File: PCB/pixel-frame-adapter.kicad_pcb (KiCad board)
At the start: 2 copper layers, 38.9 x 41.9 mm, 4 parts, among them U1 Adafruit_1_54in_TFT, U2 Adafruit_ItsyBitsy_M4, U3 Adafruit_LIS3DH

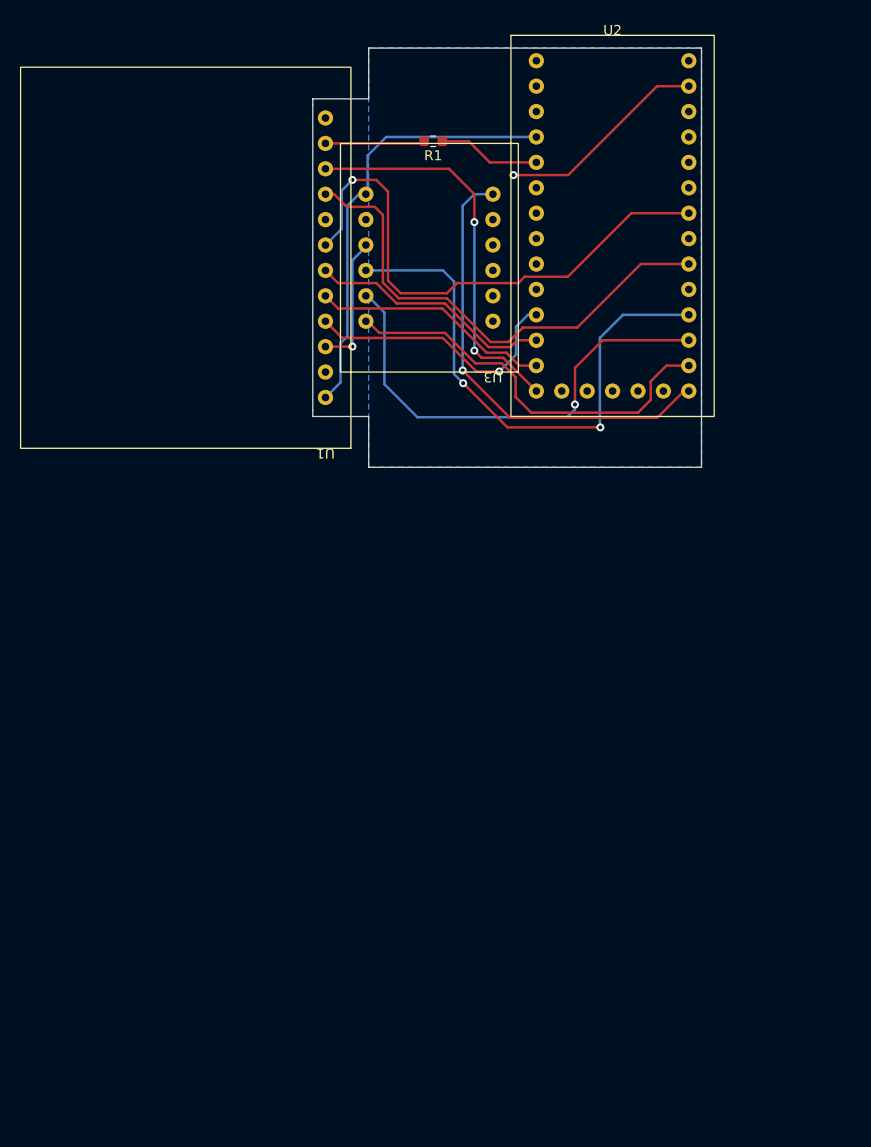
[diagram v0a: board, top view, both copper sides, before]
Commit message: rotate USB port
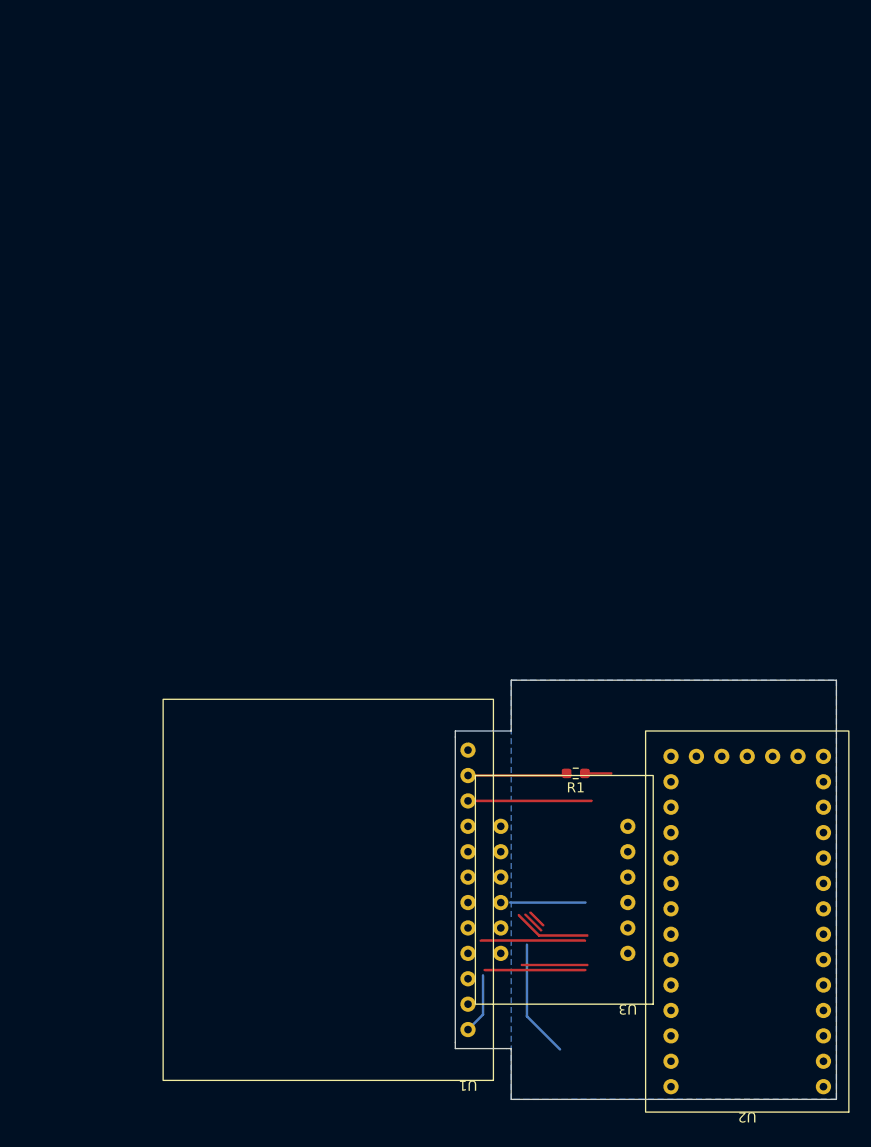
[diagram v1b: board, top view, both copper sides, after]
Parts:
- moved U2 108.5 mm to (160.8, 122.9), turned to 180 degrees
- moved R1 64.8 mm to (143.6, 89.1)
- moved U1 64.8 mm to (132.9, 119.7)
- moved U3 64.6 mm to (148.8, 112.1)
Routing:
- net SPI_CS: track 54.5 -> 1.80 mm, vias 1 -> 0
- net SPI_DC: track 49.6 -> 2.23 mm
- net I2C_SCL: track 54.0 -> 7.53 mm, vias 2 -> 0
- net ACC_INT2: track 46.0 -> 0.00 mm, vias 1 -> 0
- net +5V: track 44.1 -> 6.04 mm
- net I2C_SDA: track 46.9 -> 11.8 mm, vias 1 -> 0
- net GND: track 34.7 -> 0.00 mm, vias 2 -> 0
- net ACC_INT: track 40.1 -> 6.56 mm
- net SD_CARD_CS: track 39.9 -> 12.4 mm, vias 2 -> 0
- net SPI_CLK: track 27.1 -> 10.1 mm, vias 1 -> 0
- net SPI_MOSI: track 24.5 -> 7.70 mm
- net SD_CARD_MISO: track 24.0 -> 10.4 mm
- net BACKLIGHT: track 10.3 -> 2.64 mm
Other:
- board size 38.9 x 41.9 mm -> 38.1 x 41.9 mm

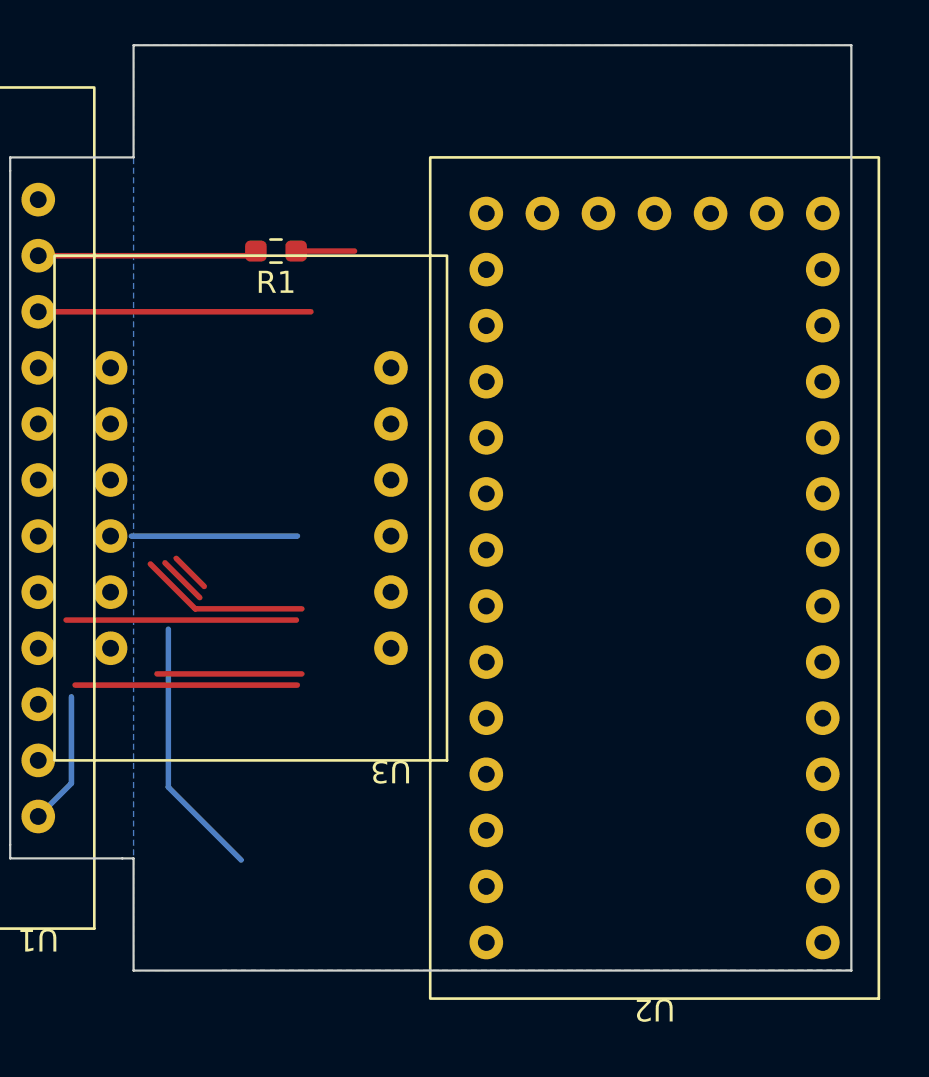
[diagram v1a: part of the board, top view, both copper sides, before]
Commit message: line up usb
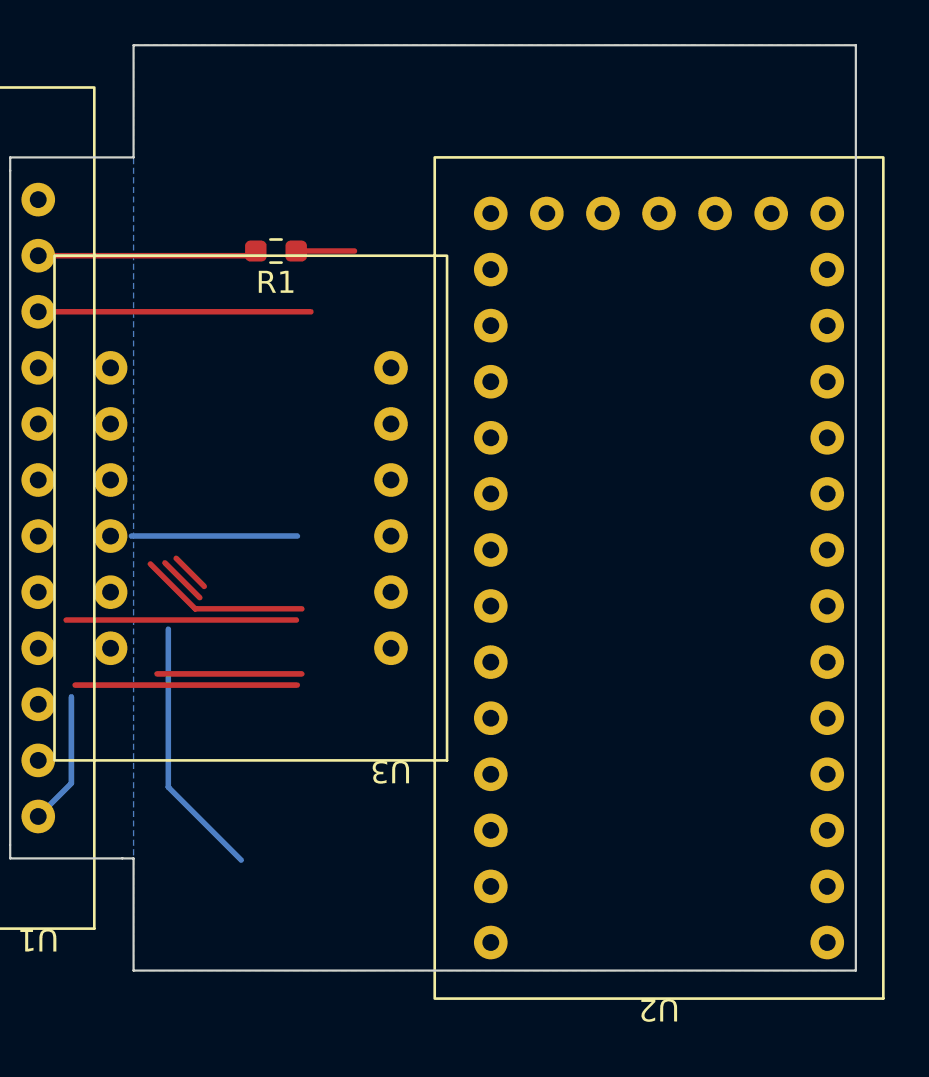
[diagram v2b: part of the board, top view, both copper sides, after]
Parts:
- moved U2 0.20 mm to (161.0, 122.9)
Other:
- board size 38.1 x 41.9 mm -> 38.3 x 41.9 mm
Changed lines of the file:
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@@
   (net 43 "unconnected-(U3-Pad8)")
   (footprint "Module:Adafruit_ItsyBitsy_M4" (layer "F.Cu")
-    (at 160.782 122.9106 180)
+    (at 160.9852 122.9106 180)
     (property "Sheetfile" "displayMotherboard.kicad_sch")
     (property "Sheetname" "")
@@
   (gr_line (start 131.5974 116.5606) (end 136.6774 116.5606) (layer "Edge.Cuts") (width 0.1))
   (gr_line (start 131.5974 84.8106) (end 131.5974 85.4202) (layer "Edge.Cuts") (width 0.1))
-  (gr_line (start 137.1854 121.6406) (end 169.6974 121.6406) (layer "Edge.Cuts") (width 0.1))
-  (gr_line (start 137.1854 79.7306) (end 169.6974 79.7306) (layer "Edge.Cuts") (width 0.1))
-  (gr_line (start 169.6974 79.7306) (end 169.6974 121.6406) (layer "Edge.Cuts") (width 0.1))
+  (gr_line (start 137.1854 121.6406) (end 169.9006 121.6406) (layer "Edge.Cuts") (width 0.1))
+  (gr_line (start 137.1854 79.7306) (end 169.9006 79.7306) (layer "Edge.Cuts") (width 0.1))
+  (gr_line (start 169.9006 79.7306) (end 169.9006 121.6406) (layer "Edge.Cuts") (width 0.1))
   (gr_line (start 137.1854 116.5606) (end 137.1854 121.6406) (layer "Edge.Cuts") (width 0.1))
   (segment (start 144.5495 89.0524) (end 147.193 89.0524) (width 0.25) (layer "F.Cu") (net 1))
@@
     (polygon
       (pts
-        (xy 169.6974 121.6152)
+        (xy 169.9006 121.6406)
         (xy 137.1854 121.6406)
         (xy 137.1854 79.7306)
-        (xy 169.6974 79.7306)
+        (xy 169.9006 79.7306)
       )
     )

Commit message: routing done
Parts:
- removed R1: 0, Resistor_SMD:R_0603_1608Metric_Pad0.98x0.95mm_HandSolder
- added JP1: SolderJumper_2_Bridged, Jumper:SolderJumper-2_P1.3mm_Bridged_RoundedPad1.0x1.5mm, F.Cu at (141.1, 85.7)
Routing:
- net +5V: track 6.04 -> 65.9 mm, vias 0 -> 1
- net SD_CARD_MISO: track 10.4 -> 66.2 mm, vias 0 -> 2
- net SPI_MOSI: track 7.70 -> 61.9 mm, vias 0 -> 3
- net SPI_CLK: track 10.1 -> 62.4 mm, vias 0 -> 2
- net BACKLIGHT: track 2.64 -> 50.2 mm, vias 0 -> 2
- net ACC_INT: track 6.56 -> 34.0 mm, vias 0 -> 2
- net SD_CARD_CS: track 12.4 -> 39.3 mm
- net SPI_CS: track 1.80 -> 27.7 mm, vias 0 -> 2
- net SPI_DC: track 2.23 -> 22.9 mm
- net I2C_SDA: track 11.8 -> 28.8 mm, vias 0 -> 2
- net I2C_SCL: track 7.53 -> 23.3 mm, vias 0 -> 2
- net ACC_INT2: track 0.00 -> 11.5 mm, vias 0 -> 1
- net Net-(JP1-Pad2): track 9.94 -> 9.08 mm

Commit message: small re-route
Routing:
- net SD_CARD_CS: track 39.3 -> 40.1 mm
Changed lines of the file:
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@@
   (segment (start 134.1308 95.6056) (end 133.8547 95.3295) (width 0.25) (layer "F.Cu") (net 9))
   (segment (start 150.0124 98.1456) (end 142.2908 98.1456) (width 0.25) (layer "F.Cu") (net 9))
+  (segment (start 144.8054 88.3666) (end 147.8788 85.2932) (width 0.25) (layer "F.Cu") (net 10))
   (segment (start 133.6736 91.8022) (end 132.8674 91.8022) (width 0.25) (layer "F.Cu") (net 10))
-  (segment (start 145.4404 87.7316) (end 147.8788 85.2932) (width 0.25) (layer "F.Cu") (net 10))
-  (segment (start 137.7442 87.7316) (end 133.6736 91.8022) (width 0.25) (layer "F.Cu") (net 10))
   (segment (start 166.5478 85.2932) (end 168.6052 87.3506) (width 0.25) (layer "F.Cu") (net 10))
   (segment (start 147.8788 85.2932) (end 166.5478 85.2932) (width 0.25) (layer "F.Cu") (net 10))
-  (segment (start 137.7442 87.7316) (end 145.4404 87.7316) (width 0.25) (layer "F.Cu") (net 10))
+  (segment (start 136.874 91.8022) (end 140.3096 88.3666) (width 0.25) (layer "F.Cu") (net 10))
+  (segment (start 132.8674 91.8022) (end 136.874 91.8022) (width 0.25) (layer "F.Cu") (net 10))
+  (segment (start 140.3096 88.3666) (end 144.8054 88.3666) (width 0.25) (layer "F.Cu") (net 10))
   (segment (start 153.3652 87.3506) (end 148.844 87.3506) (width 0.25) (layer "F.Cu") (net 25))
   (via (at 148.844 87.3506) (size 0.8) (drill 0.4) (layers "F.Cu" "B.Cu") (net 25))

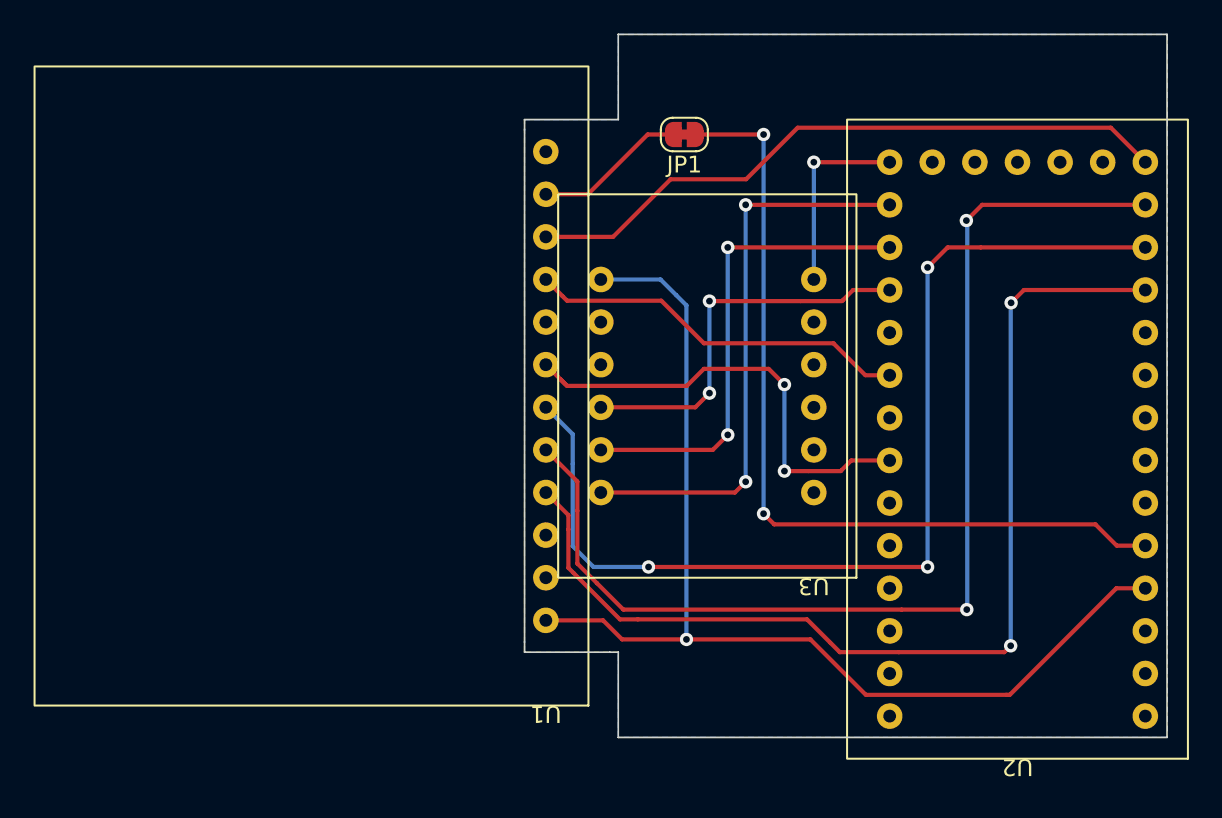
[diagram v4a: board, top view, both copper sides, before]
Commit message: dimensions and track cleanup
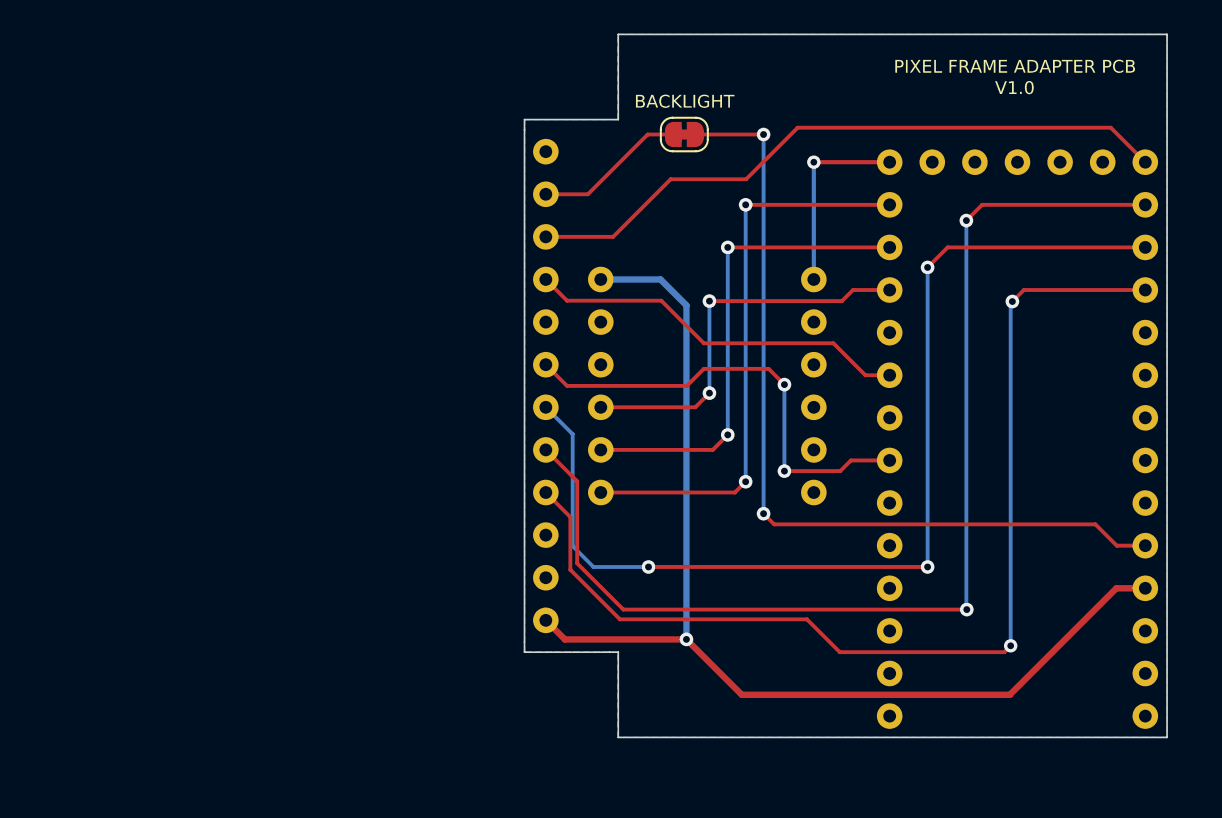
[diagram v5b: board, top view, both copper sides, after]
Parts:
- JP1: footprint Jumper:SolderJumper-2_P1.3mm_Bridged_RoundedPad1.0x1.5mm -> pixel-frame-library:SolderJumper-2_P1.3mm_Bridged_RoundedPad1.0x1.5mm
- U1: footprint Display:Adafruit_2_54in_TFT_Display -> pixel-frame-library:Adafruit_2_54in_TFT_Display
- U2: footprint Module:Adafruit_ItsyBitsy_M4 -> pixel-frame-library:Adafruit_ItsyBitsy_M4
- U3: footprint Sensor_Motion:Adafruit_LIS3DH -> pixel-frame-library:Adafruit_LIS3DH
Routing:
- net SD_CARD_CS: track 40.1 -> 39.3 mm
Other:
- board text added: "BACKLIGHT"
- board text added: "PIXEL FRAME ADAPTER PCB"
- board text added: "V1.0"

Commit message: silkscreen
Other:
- board text added: "+5V"
- board text added: "ADAFRUIT ITSYBITSY MOTHERBOARD"
- board text added: "GND"
- board text added: "LIS3DH ACCELEROMETER"
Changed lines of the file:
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@@
   (gr_line (start 169.9006 79.7306) (end 169.9006 121.6406) (layer "Edge.Cuts") (width 0.1))
   (gr_line (start 137.1854 116.5606) (end 137.1854 121.6406) (layer "Edge.Cuts") (width 0.1))
+  (gr_text "GND" (at 135.4328 109.5502) (layer "F.SilkS")
+    (effects (font (size 0.762 0.762) (thickness 0.1905)))
+  )
   (gr_text "V1.0" (at 160.8328 82.931) (layer "F.SilkS")
+    (effects (font (size 0.762 0.762) (thickness 0.1905)))
+  )
+  (gr_text "+5V" (at 135.4328 114.6302) (layer "F.SilkS")
     (effects (font (size 0.762 0.762) (thickness 0.1905)))
   )
@@
     (effects (font (size 0.762 0.762) (thickness 0.1905)))
   )
+  (gr_text "ADAFRUIT ITSYBITSY MOTHERBOARD" (at 160.9344 103.886 90) (layer "F.SilkS")
+    (effects (font (size 0.762 0.762) (thickness 0.1905)))
+  )
+  (gr_text "LIS3DH ACCELEROMETER" (at 142.494 100.6348 90) (layer "F.SilkS")
+    (effects (font (size 0.762 0.762) (thickness 0.1905)))
+  )
